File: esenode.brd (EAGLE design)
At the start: 100 x 80 mm, 11 parts, among them Q1 CSTCR6M00G53Z, U1 LPC11U6XJBD48, U2 RFM95W-868S2

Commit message: #challenge, then connect gpio to top bar and see if still possible lol
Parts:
- removed LD1: 67-23SDRSUGSUBC/TR8, everlight:PLCC4
- removed R3, R4: 10, eagle-ltspice:R0603
- removed U2: RFM95W-868S2, RFM95W-868S2:XCVR_RFM95W-868S2
- added C1: 1U, rcl:C0805
- added S1, S2: DTSM-6, switch-tact:DTSM-6
- added SV1, SV3: (no value), con-lstb:MA09-1
- added SV2: (no value), con-lstb:MA12-1
- R1: value 1U -> 10k; device resistor:R0603 -> rcl:M0805
- R2: value 56 -> 10k; device eagle-ltspice:R0603 -> rcl:M0805
- U1: value LPC11U6XJBD48 -> LPC11U68JBD64; device NXP_60_26022015:SOT313-2 -> NXP_60_26022015:SOT314-2
- moved R1 79.4 mm to (36.7, 10.3)
- moved U$1 70.4 mm to (21.5, 1.40), turned to 90 degrees
- moved U$2 64.1 mm to (17.7, 9.02), turned to 180 degrees
- moved R2 62.2 mm to (12.5, 10.3)
- moved U1 55.9 mm to (24.1, 30.5)
- moved Q1 44.9 mm to (14.0, 30.5), turned to 270 degrees
- moved U$3 17.0 mm to (14.0, 35.6), flipped to the bottom, turned to 180 degrees
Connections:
- net N$5 renamed VIN
- removed net +3V3: LD1.2, R1.1, U$2.2, U$3.VCC, U1.40, U1.44, U1.47, U1.8
- removed net 3_3V: U2.13
- removed net BLUE: R4.1, U1.21
- removed net GREEN: R3.1, U1.12
- removed net N$1: Q1.1, U1.6
- removed net N$2: Q1.3, U1.7
- removed net N$3: U$1.2, U1.19
- removed net N$8: LD1.3, R4.2
- removed net RED: R2.1, U1.36
- new net ANT: U$3.ANT
- new net D+: U$1.3, U1.26
- new net D-: U$1.2, U1.25
- new net INT0: U$3.DIO0, U1.61
- new net ISP_ENTRY: S2.1, U1.5
- new net N$18: SV3.3
- new net NRESET: S1.1, SV3.2, U1.4
- new net PWM0: SV1.6, U1.64
- new net PWM02: SV3.9, U1.33
- new net PWM03: SV3.8, U1.36
- new net PWM1: SV1.7, U1.16
- new net PWM2: SV1.8, U1.27
- new net PWM3: SV1.9, U1.49
- new net RX1: SV1.2, U1.45
- new net SCL0: SV1.4, U1.20
- new net SDA0: SV1.5, U1.21
- new net TX1: SV1.3, U1.46
- new net VCC: C1.2, R1.2, R2.2, SV1.1, U$2.2, U$3.VCC, U1.10, U1.19, U1.34, U1.53, U1.58, U1.59, U1.63
- new net XIN: Q1.1, U1.8
- new net XOUT: Q1.3, U1.9
- net GND: now also C1.1, S1.3, S1.4, S2.3, S2.4, SV3.1, U$3.GNDA, U$3.GNDB, U1.1, U1.3, U1.54, U1.57, U1.7; no longer R1.2, U1.2, U1.35, U1.41, U1.43, U1.5, U2.1, U2.10, U2.8
- net MISO0: now also SV3.5, U1.37; no longer U1.26
- net MOSI0: now also SV3.6, U1.38; no longer U1.27
- net N$4: now also U1.47; no longer U$1.3, U1.20
- net N$6: now also R2.1, S2.2; no longer LD1.1, R2.2
- net N$7: now also R1.1, S1.2; no longer LD1.4, R3.2
- net SCK0: now also SV3.4, U1.29, U1.39; no longer U1.23
- net SS0: now also SV3.7, U$3.NSS, U1.14; no longer U1.11
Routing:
- net N$9: track 0.00 -> 20.1 mm
- net N$8: track 0.00 -> 19.8 mm
- net N$5: track 0.00 -> 14.5 mm, vias 0 -> 2
- net N$16: track 0.00 -> 11.4 mm
- net N$3: track 0.00 -> 6.35 mm
- net N$14: track 0.00 -> 4.29 mm
- net N$10: track 0.00 -> 3.84 mm
- net N$11: track 0.00 -> 3.59 mm
- net N$2: track 0.00 -> 2.54 mm
- net N$1: track 0.00 -> 2.54 mm
- net N$12: track 0.00 -> 2.44 mm, vias 0 -> 1
- net N$15: track 0.00 -> 1.62 mm, vias 0 -> 1
- net N$13: track 0.00 -> 1.12 mm
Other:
- board size 100 x 80 mm -> 160 x 100 mm

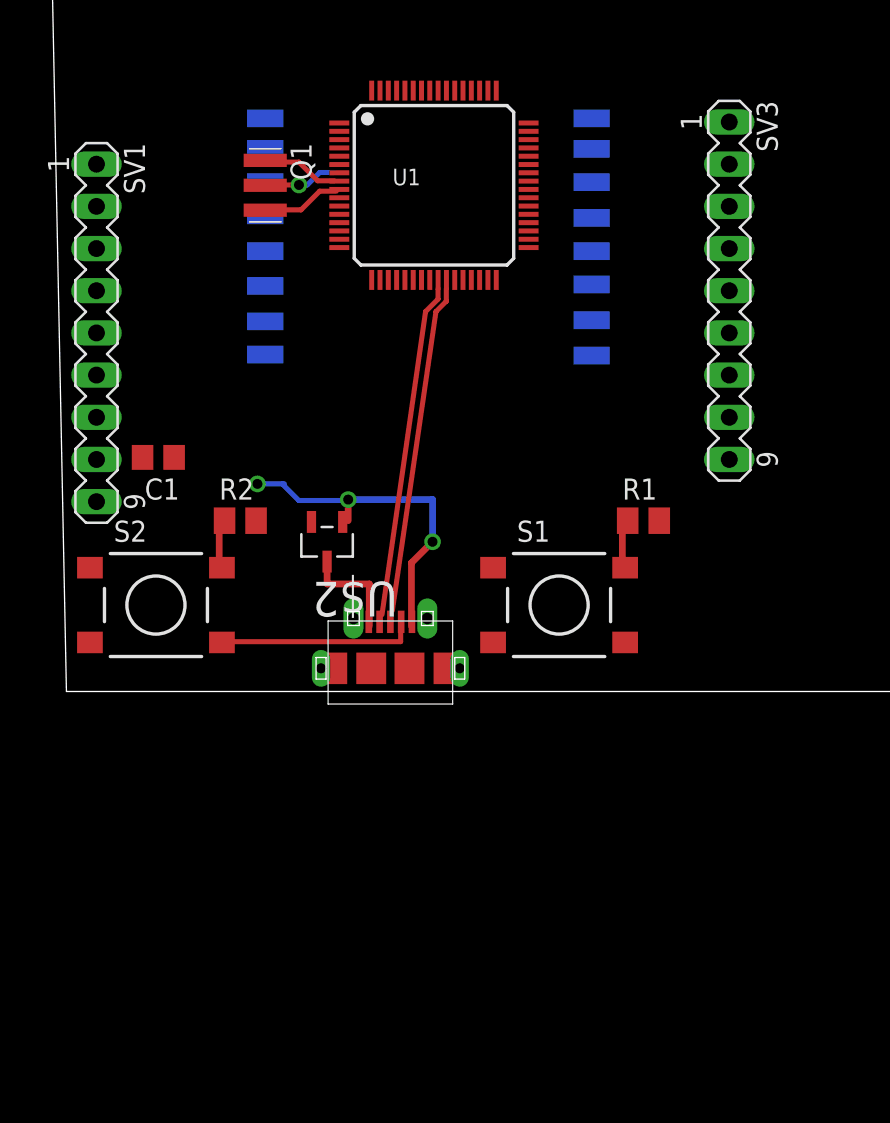
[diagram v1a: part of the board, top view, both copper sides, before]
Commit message: added antenna
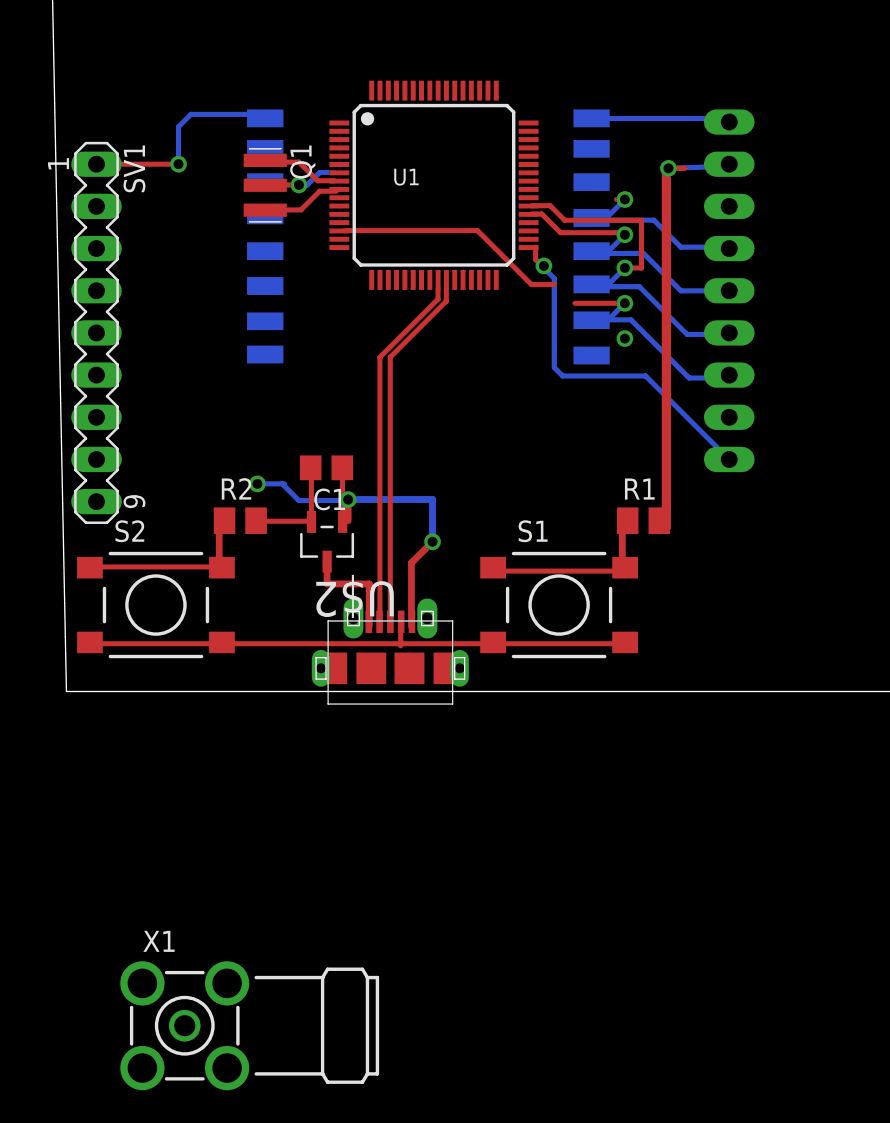
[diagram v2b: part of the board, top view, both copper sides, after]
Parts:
- added X1: BU-SMA-H, con-coax:BU-SMA-H
- moved C1 10.1 mm to (17.7, 13.5)
- flipped SV3 to the bottom
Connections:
- removed net N$6: R2.1, S2.2
- removed net N$7: R1.1, S1.2
- net ANT: now also X1.1
- net GND: now also X1.2, X1.3, X1.4, X1.5
- net ISP_ENTRY: now also R2.1, S2.2
- net NRESET: now also R1.1, S1.2
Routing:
- net N$28: track 0.00 -> 25.8 mm, vias 0 -> 1
- net N$29: track 0.00 -> 22.4 mm
- net N$31: track 0.00 -> 19.3 mm, vias 0 -> 1
- net N$6: track 0.00 -> 15.6 mm
- net N$38: track 0.00 -> 14.4 mm, vias 0 -> 1
- net N$30: track 0.00 -> 14.0 mm
- net N$26: track 0.00 -> 12.8 mm, vias 0 -> 1
- net N$32: track 0.00 -> 12.2 mm, vias 0 -> 1
- net N$25: track 0.00 -> 9.44 mm
- net N$24: track 0.00 -> 8.36 mm
- net N$27: track 0.00 -> 8.12 mm
- net N$36: track 0.00 -> 8.11 mm, vias 0 -> 1
- net N$22: track 0.00 -> 7.98 mm
- net N$21: track 0.00 -> 7.88 mm
- net N$20: track 0.00 -> 7.85 mm
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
